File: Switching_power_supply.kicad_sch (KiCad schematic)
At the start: 29 parts, among them J8 Conn_01x03_Pin, SW1 SW_DIP_x04, U4 AMS1117, U5 LM2596HVS-ADJRG

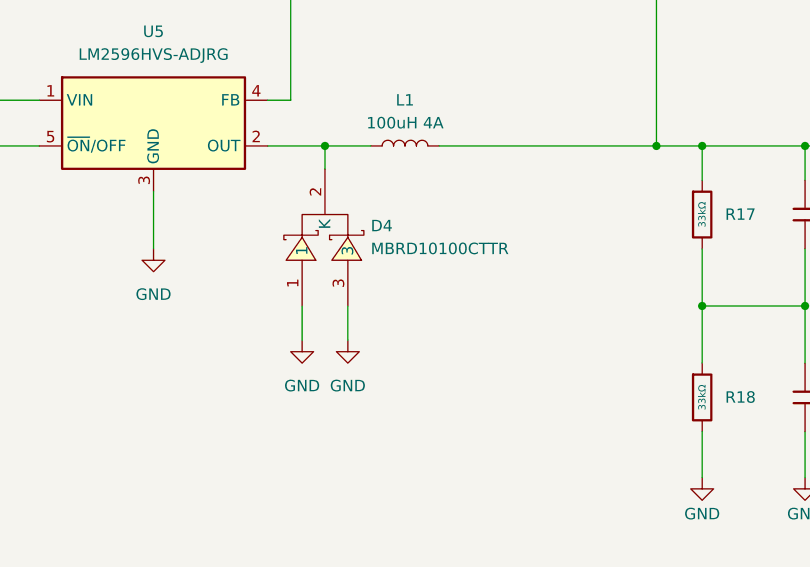
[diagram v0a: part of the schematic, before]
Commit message: added rounded corners
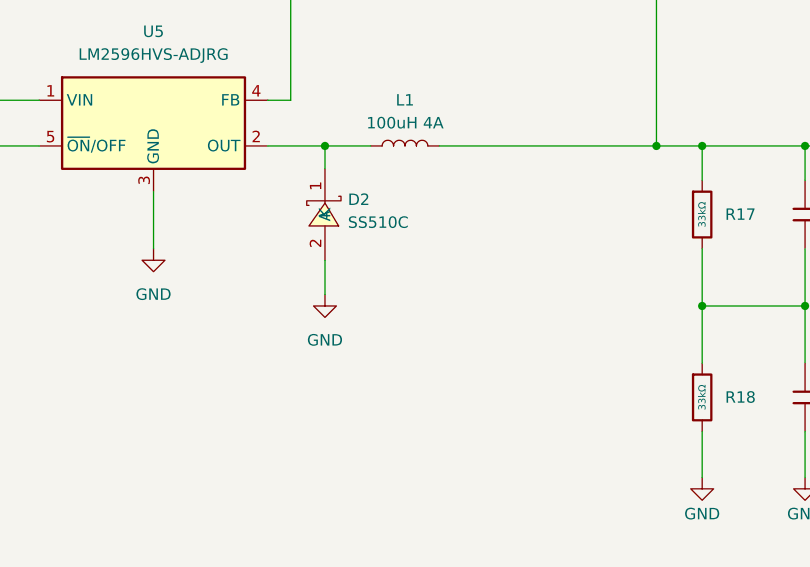
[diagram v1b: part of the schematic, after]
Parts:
- removed D4: MBRD10100CTTR, SMC_MBRD10100CTTR:TO-252-3_L6.5-W5.8-P4.58-TL, symbol SMC_MBRD10100CTTR:MBRD10100CTTR
- added D2: SS510C, SS510C:SMC_L7.1-W6.2-LS8.1-RD, symbol SS510C:SS510C
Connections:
- net GND: now also D2.2 (A)
- net at L1.1, U5.2 (OUT): now also D2.1 (K)
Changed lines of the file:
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@@
 	(wire
 		(pts
-			(xy 161.29 129.54) (xy 161.29 133.35)
-		)
-		(stroke
-			(width 0)
-			(type default)
-		)
-	)
-	(wire
-		(pts
 			(xy 261.62 82.55) (xy 261.62 78.74)
 		)
@@
 	(wire
 		(pts
-			(xy 156.21 133.35) (xy 156.21 129.54)
+			(xy 158.75 128.27) (xy 158.75 124.46)
 		)
 		(stroke
@@
 	)
 	(symbol
-		(lib_id "power:GND")
-		(at 161.29 133.35 0)
-		(unit 1)
-		(exclude_from_sim no)
-		(in_bom yes)
-		(on_board yes)
-		(dnp no)
-		(property "Reference" "#PWR085"
-			(at 161.29 139.7 0)
-			(effects
-				(font
-					(size 1.27 1.27)
-				)
-				(hide yes)
-			)
-		)
-		(property "Value" "GND"
-			(at 161.29 138.43 0)
-			(effects
-				(font
-					(size 1.27 1.27)
-				)
-			)
-		)
-		(property "Footprint" ""
-			(at 161.29 133.35 0)
-			(effects
-				(font
-					(size 1.27 1.27)
-				)
-				(hide yes)
-			)
-		)
-		(property "Datasheet" ""
-			(at 161.29 133.35 0)
-			(effects
-				(font
-					(size 1.27 1.27)
-				)
-				(hide yes)
-			)
-		)
-		(property "Description" "Power symbol creates a global label with name \"GND\" , ground"
-			(at 161.29 133.35 0)
-			(effects
-				(font
-					(size 1.27 1.27)
-				)
-				(hide yes)
-			)
-		)
-		(pin "1"
-		)
-		(instances
-			(project "MMS3_hat_stepper_controler"
-				(path "/6596548a-44e0-46d8-8624-fd71cf4a3e17/c6fe6645-c1eb-4317-9e6f-134a73c9fa05"
-					(reference "#PWR085")
-					(unit 1)
-				)
-			)
-		)
-	)
-	(symbol
 		(lib_id "power:VCC")
 		(at 50.8 109.22 180)
@@
 	)
 	(symbol
+		(lib_id "SS510C:SS510C")
+		(at 158.75 119.38 270)
+		(unit 1)
+		(exclude_from_sim no)
+		(in_bom yes)
+		(on_board yes)
+		(dnp no)
+		(fields_autoplaced yes)
+		(property "Reference" "D2"
+			(at 161.29 117.7299 90)
+			(effects
+				(font
+					(size 1.27 1.27)
+				)
+				(justify left)
+			)
+		)
+		(property "Value" "SS510C"
+			(at 161.29 120.2699 90)
+			(effects
+				(font
+					(size 1.27 1.27)
+				)
+				(justify left)
+			)
+		)
+		(property "Footprint" "SS510C:SMC_L7.1-W6.2-LS8.1-RD"
+			(at 151.13 119.38 0)
+			(effects
+				(font
+					(size 1.27 1.27)
+				)
+				(hide yes)
+			)
+		)
+		(property "Datasheet" "https://lcsc.com/product-detail/Schottky-Barrier-Diodes-SBD_SS510C_C123944.html"
+			(at 148.59 119.38 0)
+			(effects
+				(font
+					(size 1.27 1.27)
+				)
+				(hide yes)
+			)
+		)
+		(property "Description" ""
+			(at 158.75 119.38 0)
+			(effects
+				(font
+					(size 1.27 1.27)
+				)
+				(hide yes)
+			)
+		)
+		(property "Manufacturer" "晶导微电子"
+			(at 146.05 119.38 0)
+			(effects
+				(font
+					(size 1.27 1.27)
+				)
+				(hide yes)
+			)
+		)
+		(property "MPN" "SS510C"
+			(at 143.51 119.38 0)
+			(effects
+				(font
+					(size 1.27 1.27)
+				)
+				(hide yes)
+			)
+		)
+		(property "LCSC Part" "C123944"
+			(at 140.97 119.38 0)
+			(effects
+				(font
+					(size 1.27 1.27)
+				)
+				(hide yes)
+			)
+		)
+		(pin "2"
+		)
+		(pin "1"
+		)
+		(instances
+			(project "MMS3_hat_templates"
+				(path "/6596548a-44e0-46d8-8624-fd71cf4a3e17/c6fe6645-c1eb-4317-9e6f-134a73c9fa05"
+					(reference "D2")
+					(unit 1)
+				)
+			)
+		)
+	)
+	(symbol
 		(lib_id "power:+5V")
 		(at 266.7 111.76 270)
@@
 	(symbol
 		(lib_id "power:GND")
-		(at 156.21 133.35 0)
+		(at 158.75 128.27 0)
 		(unit 1)
 		(exclude_from_sim no)
@@
 		(fields_autoplaced yes)
 		(property "Reference" "#PWR084"
-			(at 156.21 139.7 0)
+			(at 158.75 134.62 0)
 			(effects
 				(font
@@
 		)
 		(property "Value" "GND"
-			(at 156.21 138.43 0)
+			(at 158.75 133.35 0)
 			(effects
 				(font
@@
 		)
 		(property "Footprint" ""
-			(at 156.21 133.35 0)
+			(at 158.75 128.27 0)
 			(effects
 				(font
@@
 		)
 		(property "Datasheet" ""
-			(at 156.21 133.35 0)
+			(at 158.75 128.27 0)
 			(effects
 				(font
@@
 		)
 		(property "Description" "Power symbol creates a global label with name \"GND\" , ground"
-			(at 156.21 133.35 0)
+			(at 158.75 128.27 0)
 			(effects
 				(font
@@
 					(unit 1)
 				)
-			)
-		)
-	)
-	(symbol
-		(lib_id "SMC_MBRD10100CTTR:MBRD10100CTTR")
-		(at 158.75 121.92 90)
-		(unit 1)
-		(exclude_from_sim no)
-		(in_bom yes)
-		(on_board yes)
-		(dnp no)
-		(fields_autoplaced yes)
-		(property "Reference" "D4"
-			(at 163.83 120.6499 90)
-			(effects
-				(font
-					(size 1.27 1.27)
-				)
-				(justify right)
-			)
-		)
-		(property "Value" "MBRD10100CTTR"
-			(at 163.83 123.1899 90)
-			(effects
-				(font
-					(size 1.27 1.27)
-				)
-				(justify right)
-			)
-		)
-		(property "Footprint" "SMC_MBRD10100CTTR:TO-252-3_L6.5-W5.8-P4.58-TL"
-			(at 168.91 121.92 0)
-			(effects
-				(font
-					(size 1.27 1.27)
-				)
-				(hide yes)
-			)
-		)
-		(property "Datasheet" "https://lcsc.com/product-detail/Schottky-Barrier-Diodes-SBD_MCC_MBRD10100CTTR_MBRD10100CTTR_C135494.html"
-			(at 171.45 121.92 0)
-			(effects
-				(font
-					(size 1.27 1.27)
-				)
-				(hide yes)
-			)
-		)
-		(property "Description" ""
-			(at 158.75 121.92 0)
-			(effects
-				(font
-					(size 1.27 1.27)
-				)
-				(hide yes)
-			)
-		)
-		(property "LCSC Part" "C135494"
-			(at 173.99 121.92 0)
-			(effects
-				(font
-					(size 1.27 1.27)
-				)
-				(hide yes)
-			)
-		)
-		(property "Sim.Device" ""
-			(at 158.75 121.92 90)
-			(effects
-				(font
-					(size 1.27 1.27)
-				)
-				(hide yes)
-			)
-		)
-		(pin "1"
-		)
-		(pin "2"
-		)
-		(pin "3"
-		)
-		(instances
-			(project ""
-				(path "/6596548a-44e0-46d8-8624-fd71cf4a3e17/c6fe6645-c1eb-4317-9e6f-134a73c9fa05"
-					(reference "D4")
-					(unit 1)
-				)
